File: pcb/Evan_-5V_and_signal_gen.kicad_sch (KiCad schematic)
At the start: 28 parts, among them IC1 TL7660IDGKR, IC4 UA78M33CDCYG3, IC9 TL081IDT, U5 TPS2069CDBVR_MOSFET

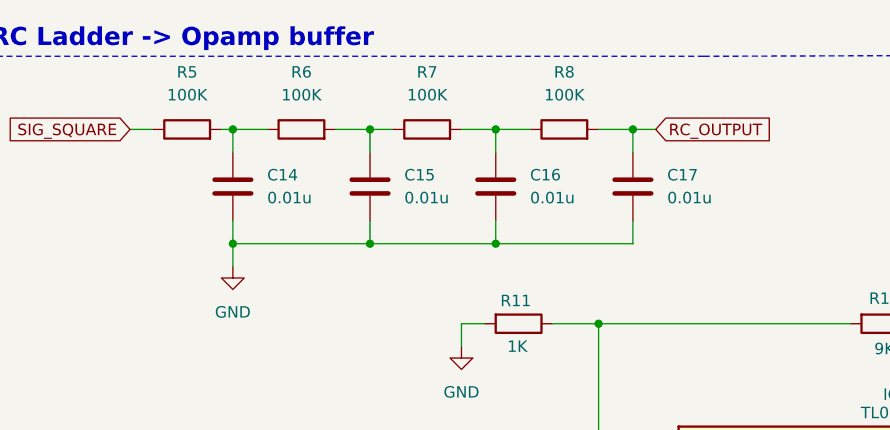
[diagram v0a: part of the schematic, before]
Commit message: Fixed silkscreen and component values
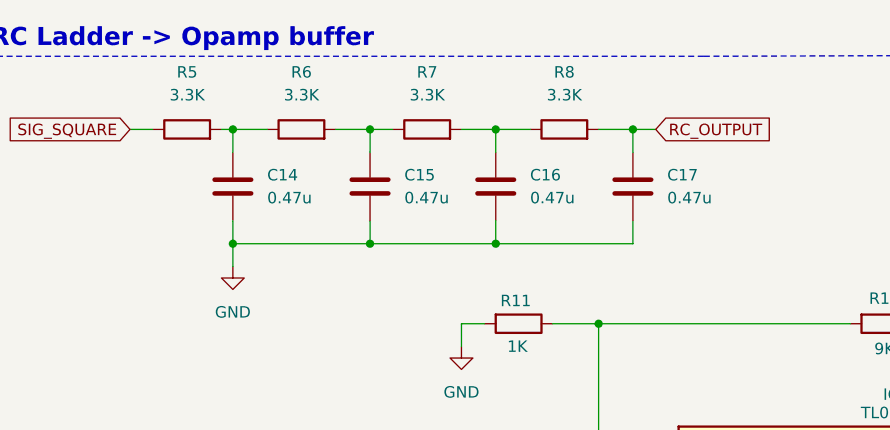
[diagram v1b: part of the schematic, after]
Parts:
- C14, C15, C16, C17: value 0.01u -> 0.47u
- R5, R6, R7, R8: value 100K -> 3.3K
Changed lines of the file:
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@@
 			)
 		)
-		(property "Value" "0.01u"
+		(property "Value" "0.47u"
 			(at 162.56 33.0199 0)
 			(effects
@@
 			)
 		)
-		(property "Value" "100K"
+		(property "Value" "3.3K"
 			(at 165.1 21.59 90)
 			(effects
@@
 			)
 		)
-		(property "Value" "0.01u"
+		(property "Value" "0.47u"
 			(at 191.77 33.0199 0)
 			(effects
@@
 			)
 		)
-		(property "Value" "0.01u"
+		(property "Value" "0.47u"
 			(at 176.53 33.0199 0)
 			(effects
@@
 			)
 		)
-		(property "Value" "100K"
+		(property "Value" "3.3K"
 			(at 180.34 21.59 90)
 			(effects
@@
 			)
 		)
-		(property "Value" "100K"
+		(property "Value" "3.3K"
 			(at 138.43 21.59 90)
 			(effects
@@
 			)
 		)
-		(property "Value" "0.01u"
+		(property "Value" "0.47u"
 			(at 147.32 33.0199 0)
 			(effects
@@
 			)
 		)
-		(property "Value" "100K"
+		(property "Value" "3.3K"
 			(at 151.13 21.59 90)
 			(effects

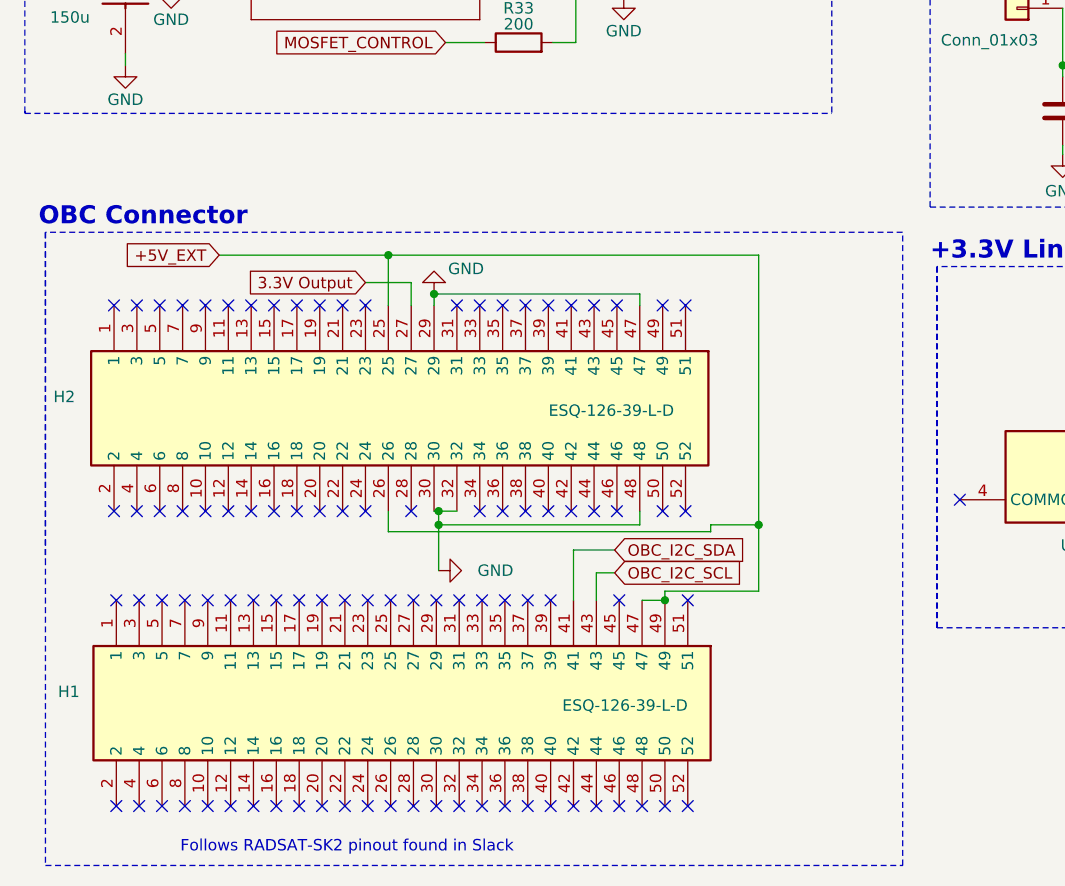
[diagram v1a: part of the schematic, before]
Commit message: Updated CSKB connector
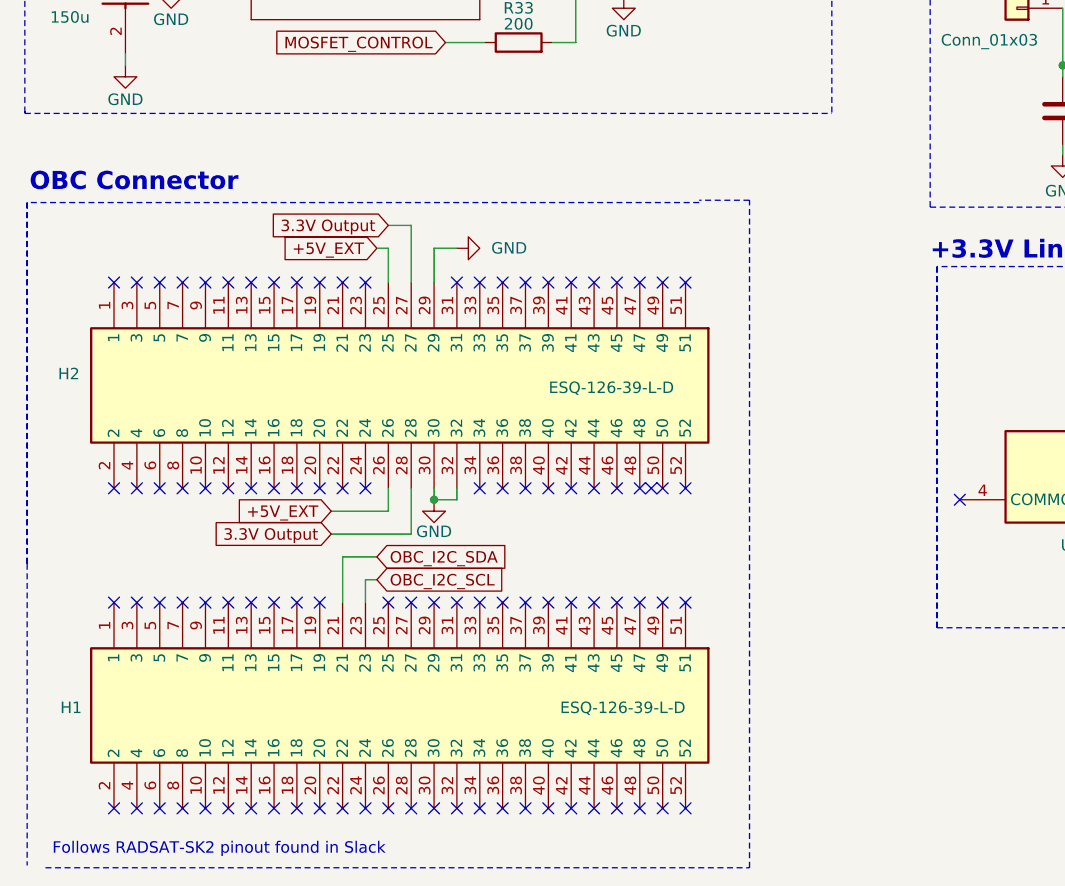
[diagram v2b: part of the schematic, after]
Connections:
- net +5V_EXT: no longer H1.47, H1.49
- net 3.3V Output: now also H2.28
- net GND: no longer H2.47, H2.48
- net OBC_I2C_SCL: now also H1.23; no longer H1.43
- net OBC_I2C_SDA: now also H1.21; no longer H1.41
- no-connect marks 97 -> 101
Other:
- moved on the sheet: H2

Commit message: Added missing decoupling capacitor + changed capacitors footprint
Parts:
- C12, C13: footprint capstone:T495D -> Capacitor_SMD:C_0805_2012Metric
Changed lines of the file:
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@@
 			)
 		)
-		(property "Footprint" "capstone:T495D"
+		(property "Footprint" "Capacitor_SMD:C_0805_2012Metric"
 			(at 173.66 45.72 0)
 			(effects
@@
 			)
 		)
-		(property "Footprint" "capstone:T495D"
+		(property "Footprint" "Capacitor_SMD:C_0805_2012Metric"
 			(at -69.266 38.862 0)
 			(effects

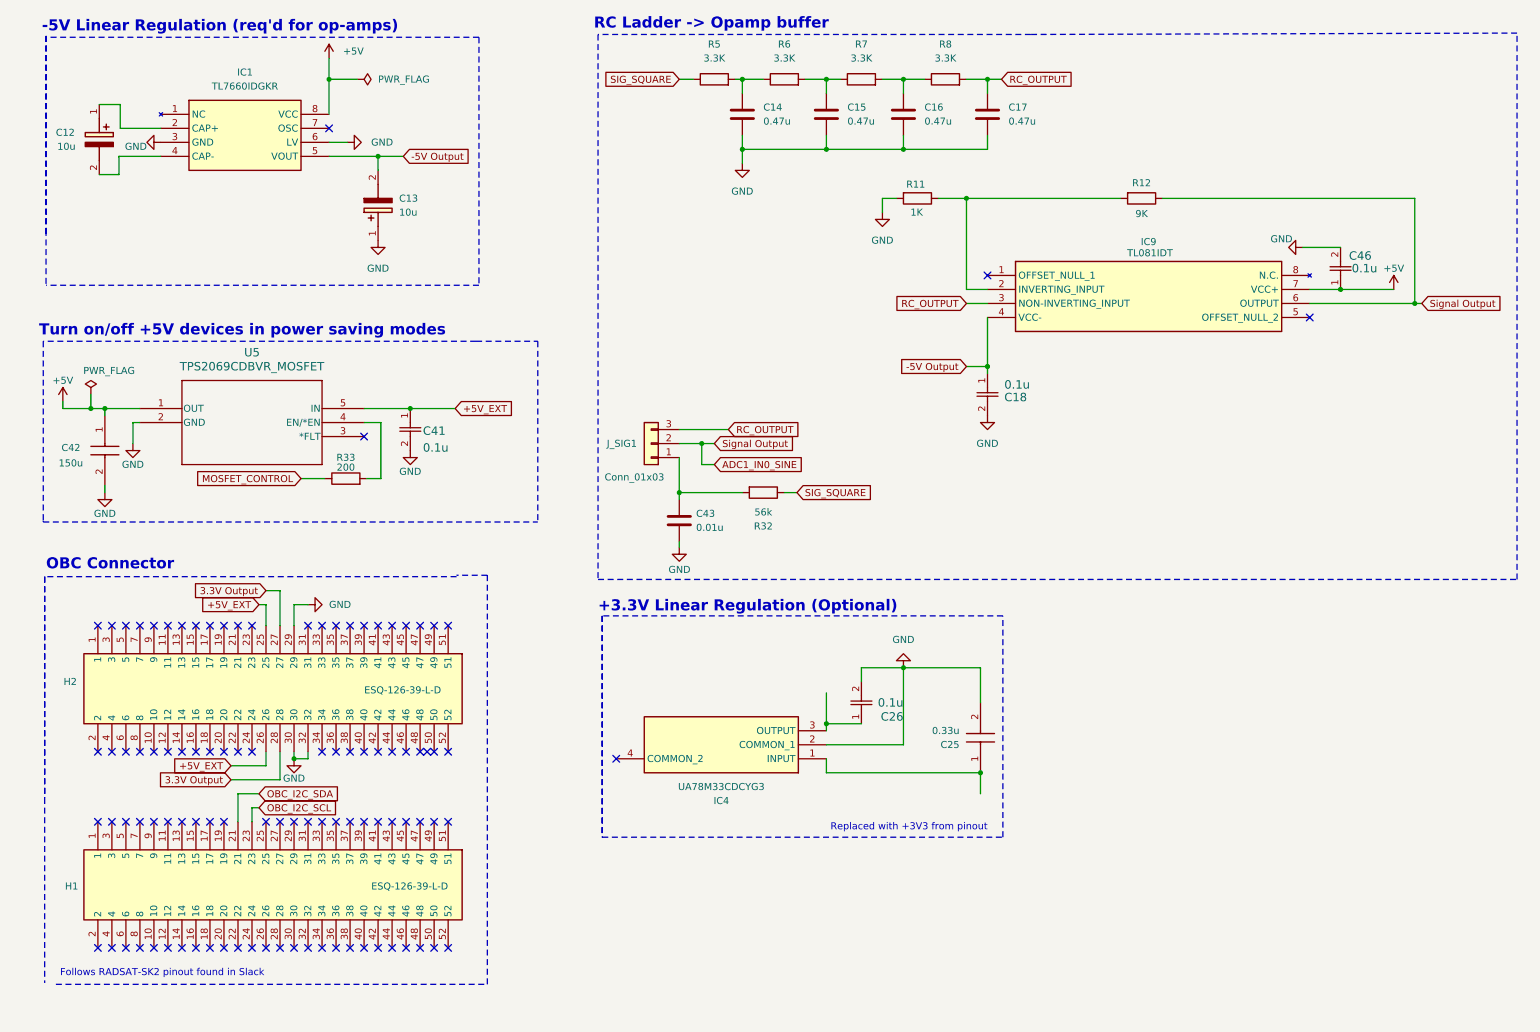
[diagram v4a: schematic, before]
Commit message: Fixed Shield Solder Mask
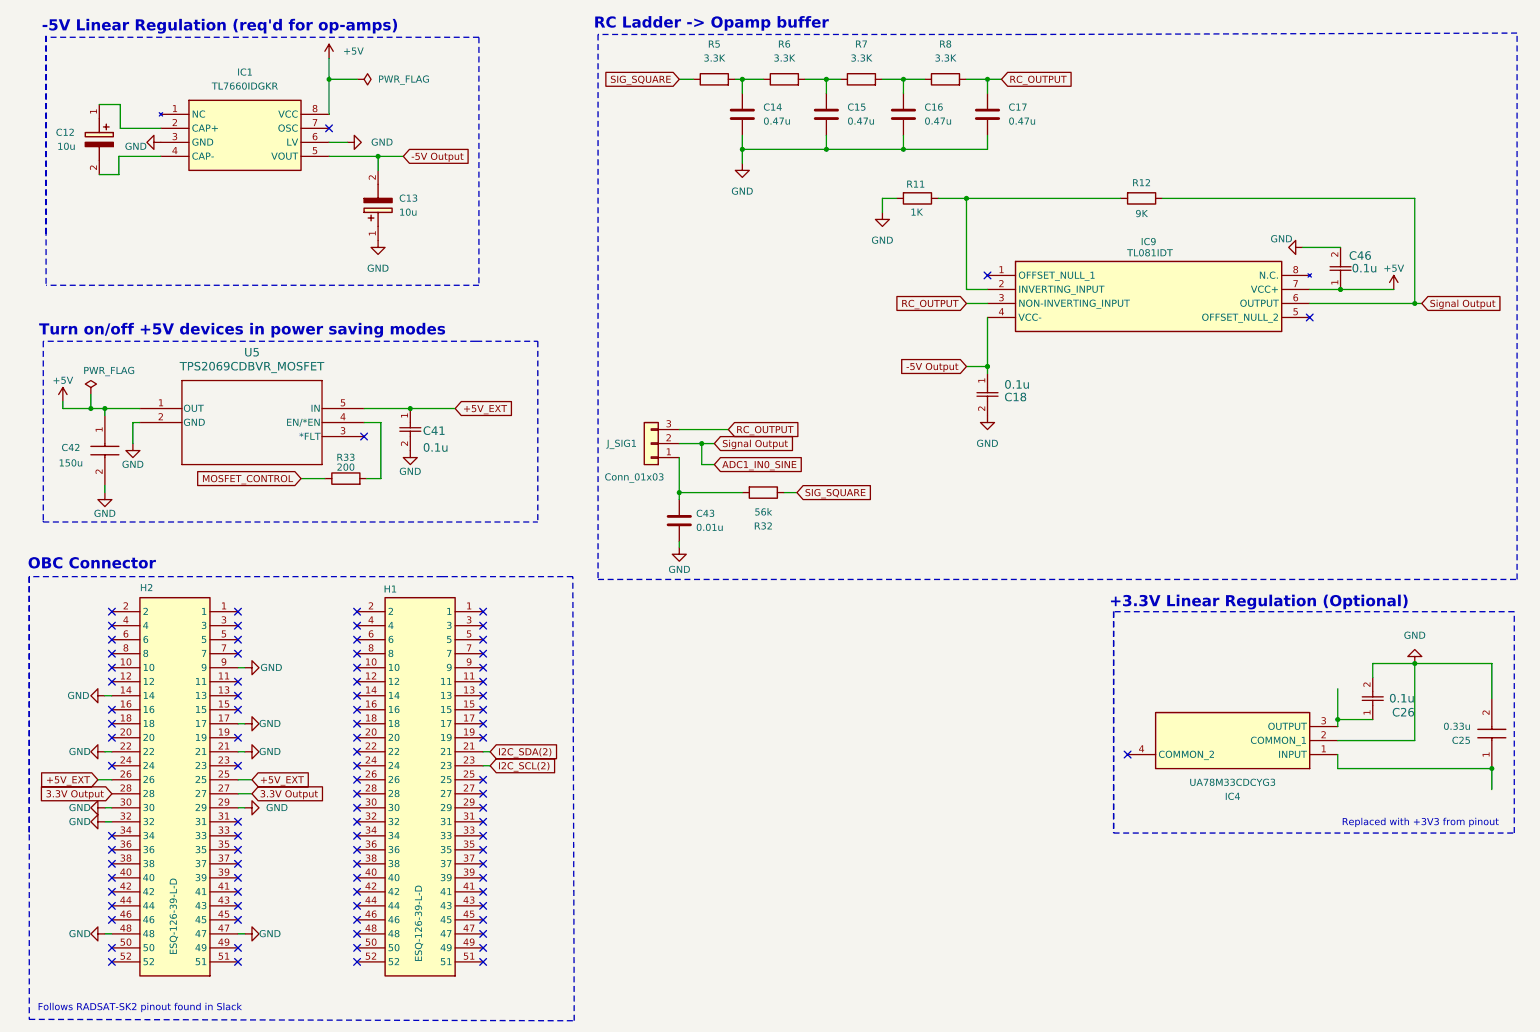
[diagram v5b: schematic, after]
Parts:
- H1, H2: footprint capstone:ESQ-126-Y-X-D -> capstone:RHDR52W64P254_2X26_6654X495X1135P
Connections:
- net GND: now also H2.14, H2.17, H2.21, H2.22, H2.47, H2.48, H2.9
- net OBC_I2C_SCL renamed I2C_SCL(2)
- net OBC_I2C_SDA renamed I2C_SDA(2)
- no-connect marks 101 -> 93
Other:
- moved on the sheet: C25, C26, H1, H2, IC4

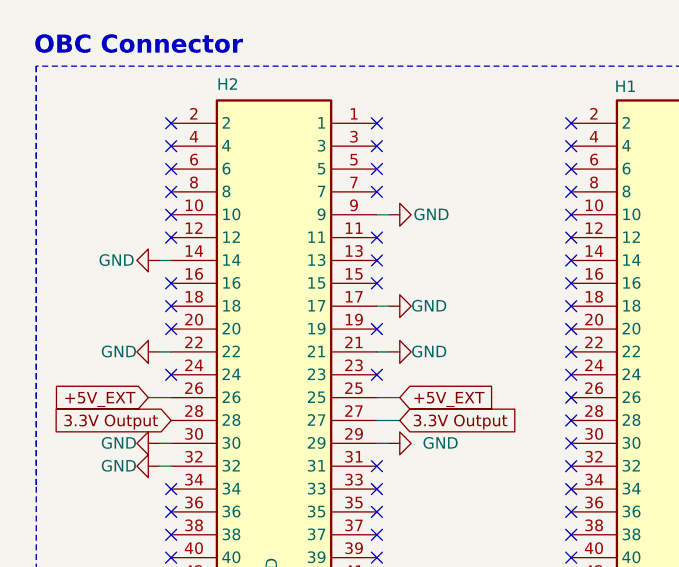
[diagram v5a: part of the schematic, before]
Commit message: Moved control IC capacitors to back of board to conform with other IC groups
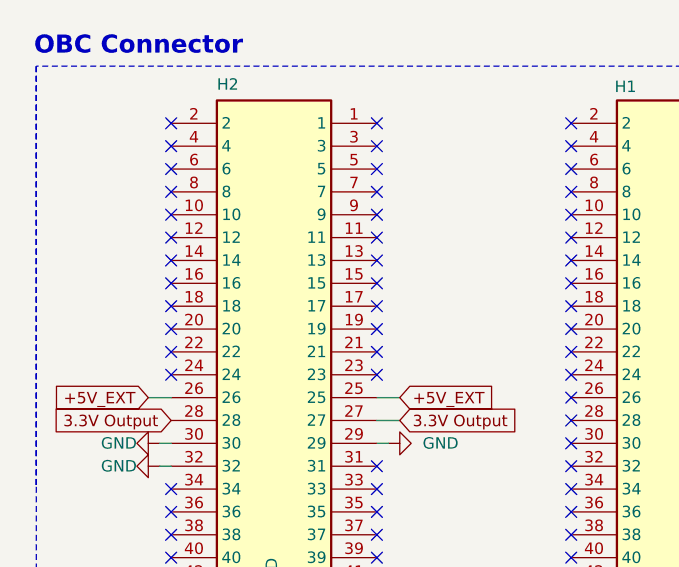
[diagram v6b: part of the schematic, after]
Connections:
- net GND: no longer H2.14, H2.17, H2.21, H2.22, H2.9
- no-connect marks 93 -> 98
